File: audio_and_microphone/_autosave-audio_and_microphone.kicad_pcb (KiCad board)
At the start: 2 copper layers, 81.7 x 60.4 mm, 23 parts, among them J10 Conn_01x02_Pin, J4 Conn_01x03_Pin, J5 Conn_01x02, J7 Conn_01x02

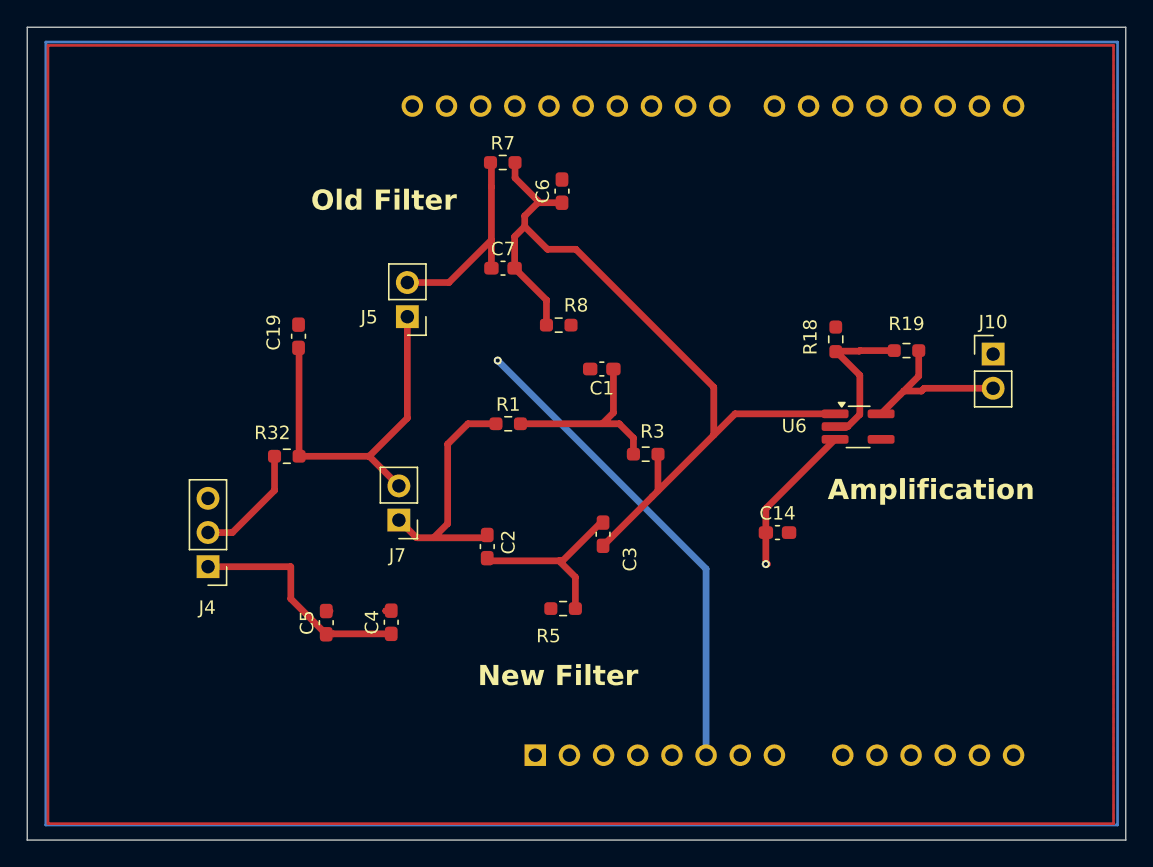
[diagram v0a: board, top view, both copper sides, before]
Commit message: added additional testing point and more silkscreen texts
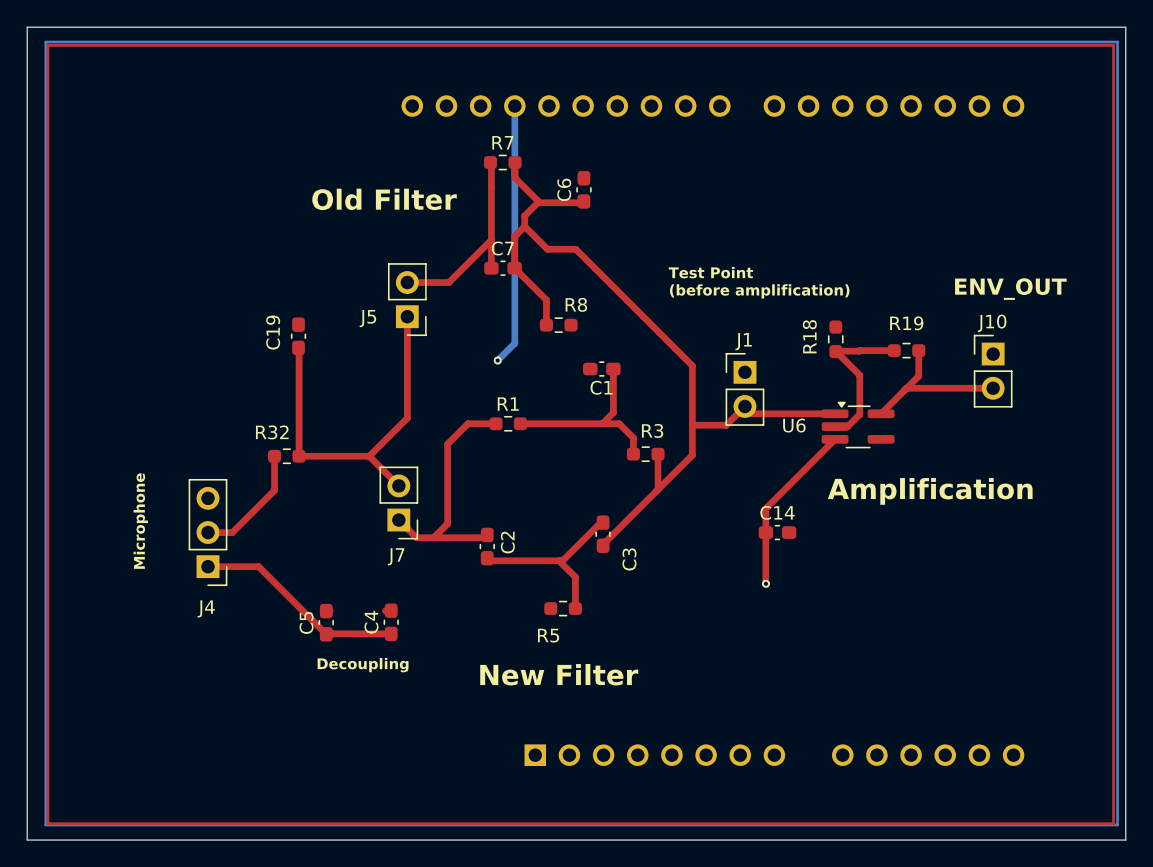
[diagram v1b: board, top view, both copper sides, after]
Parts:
- added J1: Conn_01x02_Pin, Connector_PinHeader_2.54mm:PinHeader_1x02_P2.54mm_Vertical, F.Cu at (141.0, 97.2)
- moved C6 1.64 mm to (129.1, 83.7)
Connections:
- A1 pad 29: unconnected-(A1-GND-Pad29) -> GND
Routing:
- net GND: track 36.6 -> 20.1 mm
- net /after new filter: track 62.9 -> 65.1 mm
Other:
- board text added: "Decoupling"
- board text added: "ENV_OUT"
- board text added: "Microphone"
- board text added: "Test Point (before amplification)"
